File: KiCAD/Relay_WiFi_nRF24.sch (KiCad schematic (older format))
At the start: 15 parts, among them IC1 MOC3061M, P1 CONN_4, P2 CONN_4, P3 CONN_01X04, U1 ESP8266-ESP-03, U2 NCP1117ST33T3G, U3 NRF24L01P_SMD, U4 TRIAC

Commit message: Замена посадочного места блока питания 5V
Изменил посадочное место блока питания под размеры китайского БП с
Ebay.com AC/DC-5V-700A
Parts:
- P3: footprint Converters_DCDC_ACDC:ACDC-Converter_TRACO-TMLM-05 -> Relay_WiFi_nRF24_Libs:ACDC-FromEbay-5V-700A
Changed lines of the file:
@@
 LIBS:nrf24l01p_smd
 LIBS:Conn_PWR
+LIBS:Relay_WiFi_nRF24-cache
 EELAYER 25 0
 EELAYER END
@@
 F 0 "P3" H 9150 4550 50  0000 C CNN
 F 1 "CONN_01X04" V 9250 4300 50  0000 C CNN
-F 2 "Converters_DCDC_ACDC:ACDC-Converter_TRACO-TMLM-05" H 9150 4300 60  0001 C CNN
+F 2 "Relay_WiFi_nRF24_Libs:ACDC-FromEbay-5V-700A" H 9150 4300 60  0001 C CNN
 F 3 "" H 9150 4300 60  0000 C CNN
 	1    9150 4300

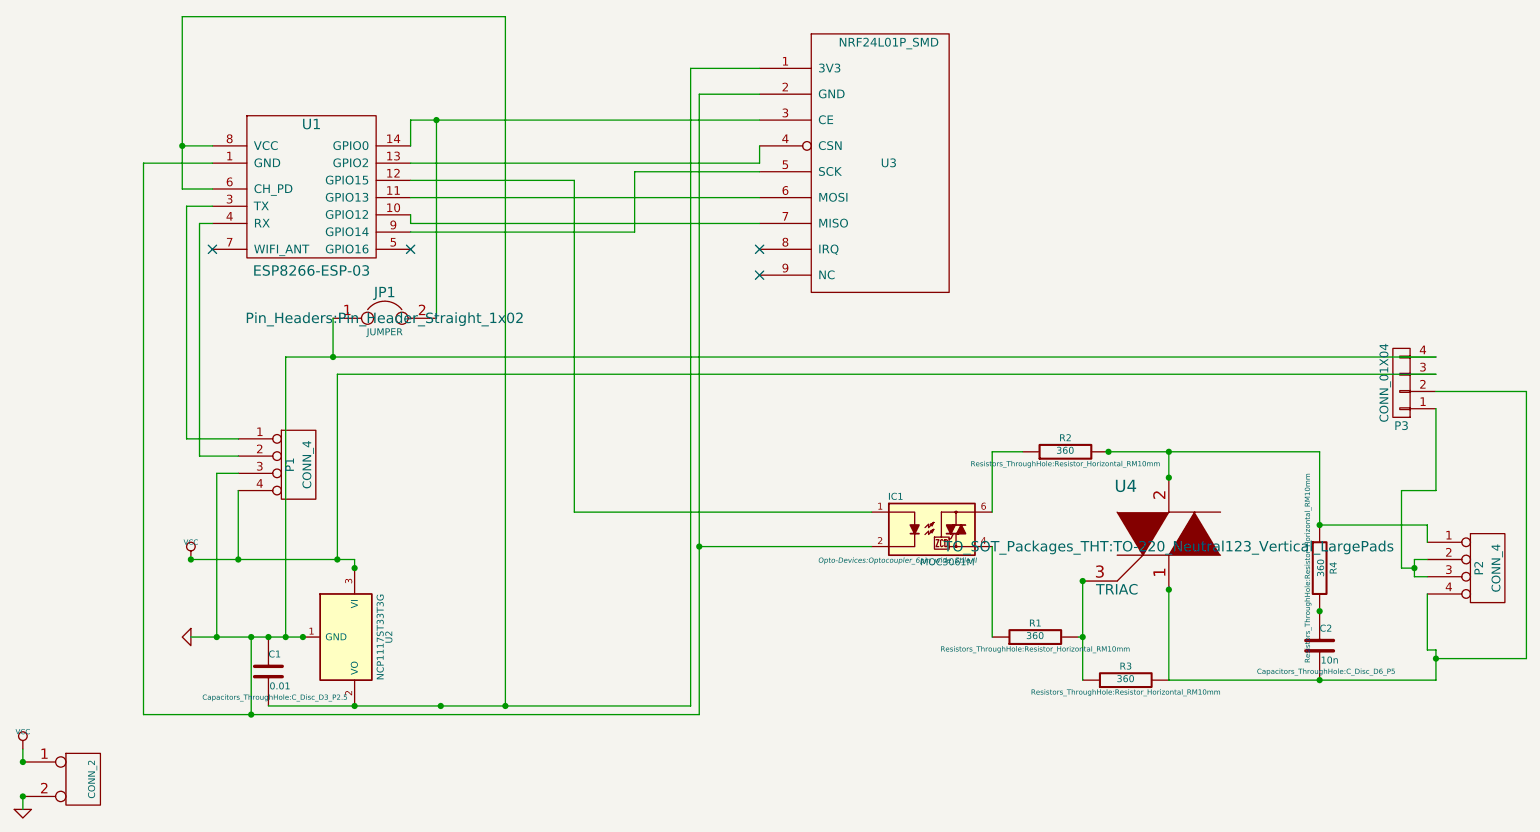
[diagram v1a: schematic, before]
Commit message: Правка схемы
Добавлены недостающие подтягивающие резисторы.
Исправлена библиотека посадочного места коннектора для подключения сети
и нагрузки.
Исправлена толщина дорожек.
Уменьшен размер платы.
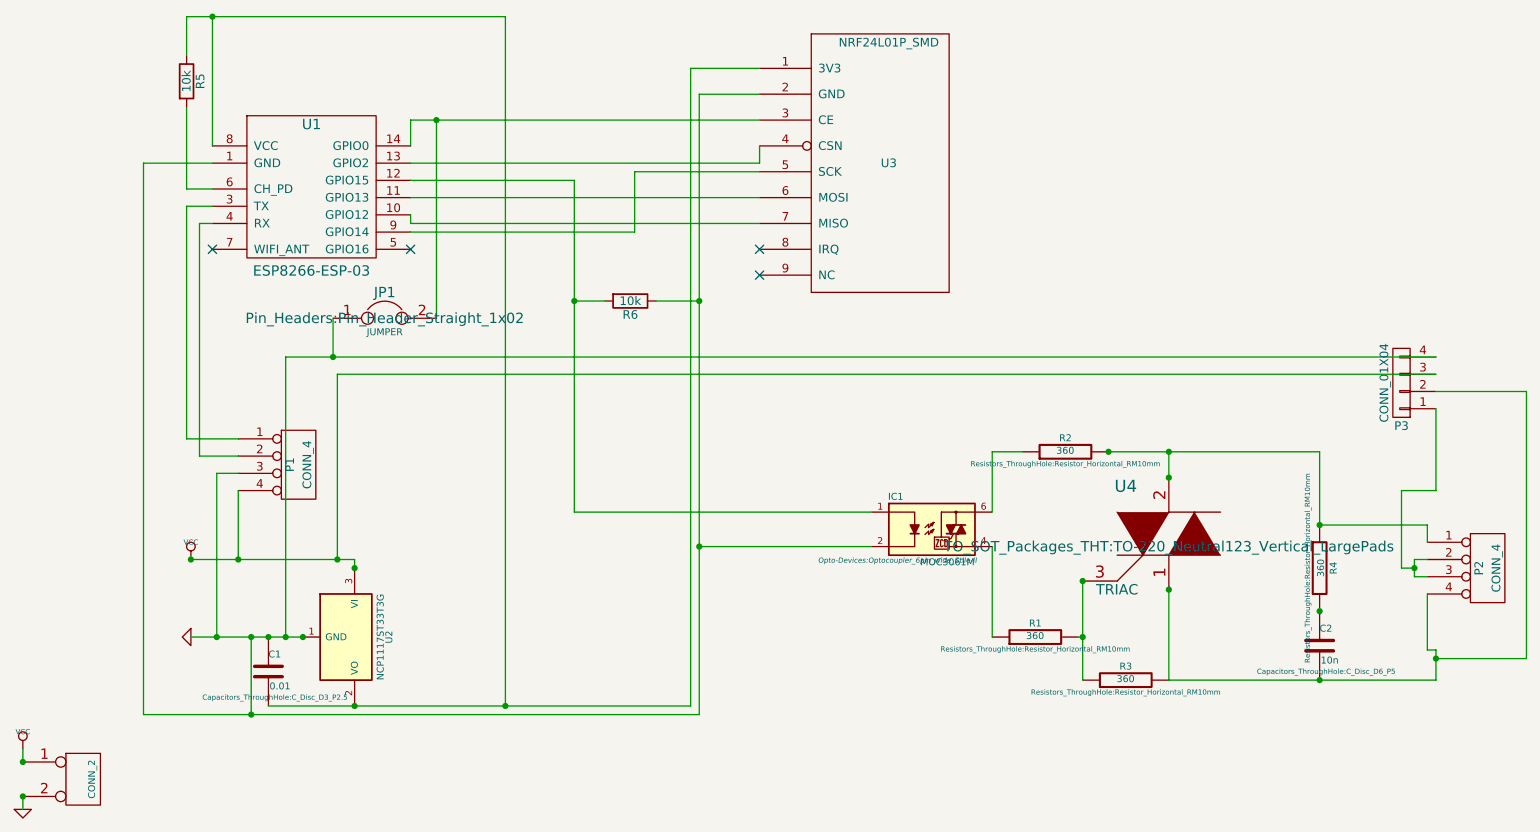
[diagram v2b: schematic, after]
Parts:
- added R5, R6: 10k, Resistors_SMD:R_0805_HandSoldering, symbol R
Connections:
- net GND: now also R6.1
- net at IC1.1, U1.12 (GPIO15): now also R6.2
- net at C1.2, U1.8 (VCC), U2.2 (VO)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: now also R5.1; no longer U1.6 (CH_PD)
- new net: R5.2, U1.6 (CH_PD)
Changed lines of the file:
@@
 	-1   0    0    1
 $EndComp
+$Comp
+L R R6
+U 1 1 562E5413
+P 4675 3825
+F 0 "R6" V 4755 3825 50  0000 C CNN
+F 1 "10k" V 4675 3825 50  0000 C CNN
+F 2 "Resistors_SMD:R_0805_HandSoldering" V 4605 3825 30  0001 C CNN
+F 3 "" H 4675 3825 30  0000 C CNN
+	1    4675 3825
+	0    1    1    0
+$EndComp
+$Comp
+L R R5
+U 1 1 562E56EC
+P 2100 2550
+F 0 "R5" V 2180 2550 50  0000 C CNN
+F 1 "10k" V 2100 2550 50  0000 C CNN
+F 2 "Resistors_SMD:R_0805_HandSoldering" V 2030 2550 30  0001 C CNN
+F 3 "" H 2100 2550 30  0000 C CNN
+	1    2100 2550
+	1    0    0    -1
+$EndComp
 Wire Wire Line
 	2575 6175 5025 6175
@@
 	3950 2175 3950 6175
 Wire Wire Line
-	2075 2175 3950 2175
-Connection ~ 3575 6175
-Wire Wire Line
-	2075 2175 2075 3175
-Wire Wire Line
-	2075 2925 2250 2925
+	2100 2175 3950 2175
 Connection ~ 3950 6175
 Wire Wire Line
@@
 	7800 6025 7800 5500
 Wire Wire Line
-	7800 6025 9350 6025
-Wire Wire Line
-	9350 6025 9350 5850
+	9350 6025 7800 6025
+Wire Wire Line
+	9350 5850 9350 6025
 Wire Wire Line
 	7800 4700 7800 4850
@@
 Connection ~ 2475 6225
 Wire Wire Line
-	2075 3175 2250 3175
-Connection ~ 2075 2925
-Wire Wire Line
 	2275 5775 2275 4825
 Wire Wire Line
@@
 	5425 3225 3400 3225
 Wire Wire Line
-	5425 2775 3400 2775
+	3400 2775 5425 2775
 Wire Wire Line
 	3400 2775 3400 2925
@@
 Connection ~ 2975 5325
 Wire Wire Line
-	9350 4150 2675 4150
+	2675 4150 9350 4150
 Wire Wire Line
 	2675 4150 2675 5775
@@
 	2950 3925 2950 4150
 Connection ~ 2950 4150
+Wire Wire Line
+	4825 3825 5075 3825
+Connection ~ 5075 3825
+Wire Wire Line
+	4525 3825 4350 3825
+Connection ~ 4350 3825
+Wire Wire Line
+	2250 2925 2250 2175
+Wire Wire Line
+	2100 2400 2100 2175
+Connection ~ 2250 2175
+Wire Wire Line
+	2100 2700 2100 3175
+Wire Wire Line
+	2100 3175 2250 3175
 $EndSCHEMATC

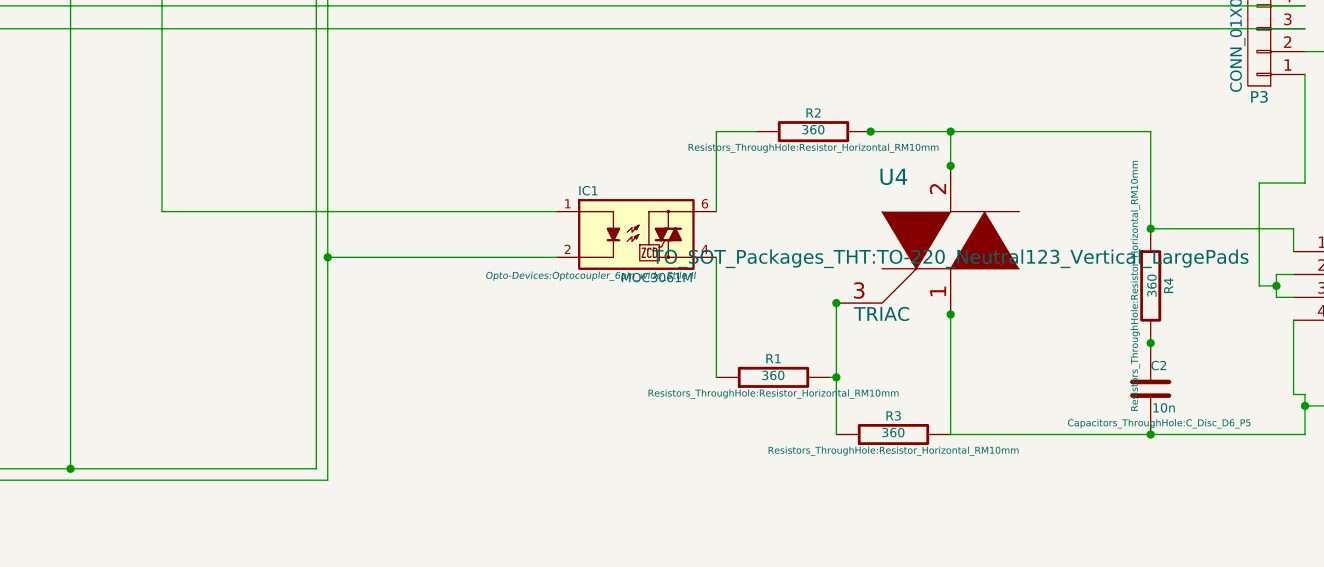
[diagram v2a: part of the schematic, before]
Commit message: Изменения в схеме
Добавлен токоограничивающий резистр.
Мелкие правки печатной платы.
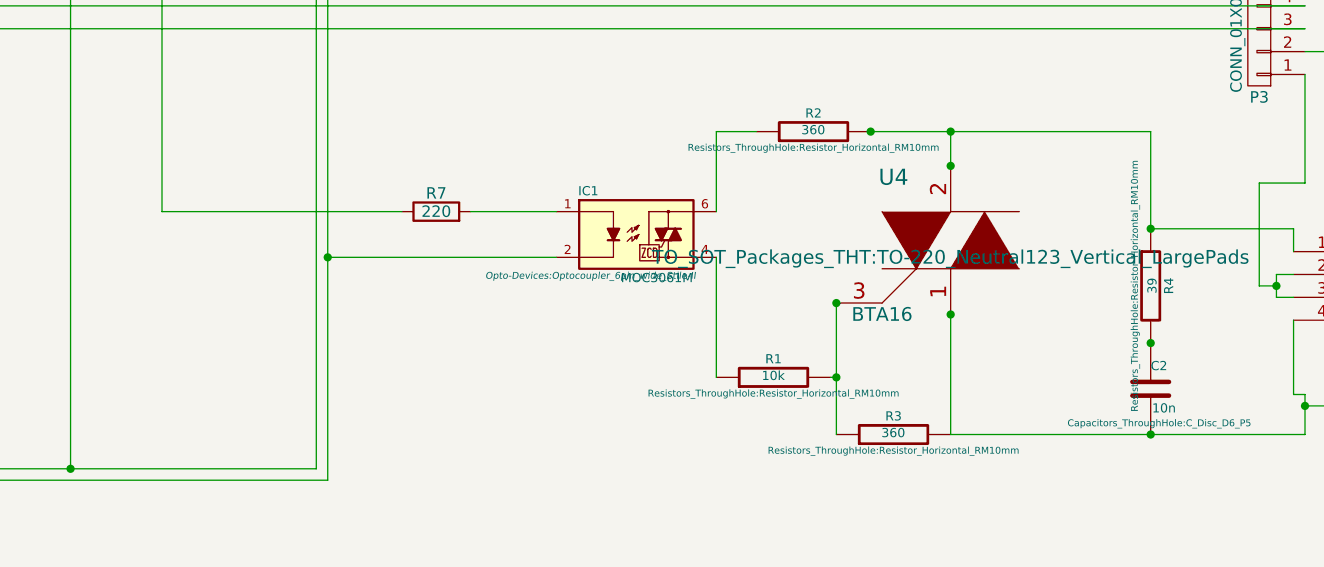
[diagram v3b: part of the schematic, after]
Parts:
- added R7: 220, Resistors_SMD:R_0805_HandSoldering, symbol R
- R1: value 360 -> 10k
- R4: value 360 -> 39
- U4: value TRIAC -> BTA16
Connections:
- net at R6.2, U1.12 (GPIO15): now also R7.1; no longer IC1.1
- new net: IC1.1, R7.2
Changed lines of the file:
@@
 P 7800 5250
 F 0 "U4" H 7550 5600 70  0000 C CNN
-F 1 "TRIAC" H 7500 5000 60  0000 C CNN
+F 1 "BTA16" H 7500 5000 60  0000 C CNN
 F 2 "TO_SOT_Packages_THT:TO-220_Neutral123_Vertical_LargePads" H 7800 5250 60  0000 C CNN
 F 3 "~" H 7800 5250 60  0000 C CNN
@@
 P 8675 5375
 F 0 "R4" V 8755 5375 40  0000 C CNN
-F 1 "360" V 8682 5376 40  0000 C CNN
+F 1 "39" V 8682 5376 40  0000 C CNN
 F 2 "Resistors_ThroughHole:Resistor_Horizontal_RM10mm" V 8605 5375 30  0000 C CNN
 F 3 "~" H 8675 5375 30  0000 C CNN
@@
 P 7025 5775
 F 0 "R1" V 7105 5775 40  0000 C CNN
-F 1 "360" V 7032 5776 40  0000 C CNN
+F 1 "10k" V 7032 5776 40  0000 C CNN
 F 2 "Resistors_ThroughHole:Resistor_Horizontal_RM10mm" V 6955 5775 30  0000 C CNN
 F 3 "~" H 7025 5775 30  0000 C CNN
@@
 	4350 3125 4350 5050
 Wire Wire Line
-	4350 5050 6075 5050
-Wire Wire Line
 	6075 5250 5075 5250
 Connection ~ 5075 5250
@@
 Wire Wire Line
 	2100 3175 2250 3175
+$Comp
+L R R7
+U 1 1 562E8BDD
+P 5550 5050
+F 0 "R7" V 5630 5050 50  0000 C CNN
+F 1 "220" V 5550 5050 50  0000 C CNN
+F 2 "Resistors_SMD:R_0805_HandSoldering" V 5480 5050 30  0001 C CNN
+F 3 "" H 5550 5050 30  0000 C CNN
+	1    5550 5050
+	0    -1   -1   0
+$EndComp
+Wire Wire Line
+	6075 5050 5700 5050
+Wire Wire Line
+	4350 5050 5400 5050
 $EndSCHEMATC
